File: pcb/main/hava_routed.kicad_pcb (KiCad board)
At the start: 2 copper layers, 32 x 41 mm, 24 parts, among them J1 USB_C_Receptacle_USB2.0_16P, J2 Conn_01x04, SW1 SW_Push, SW2 SW_Push, U1 ESP32-C3-WROOM-02, U2 AP2112K-3.3, U4 USBLC6-2SC6

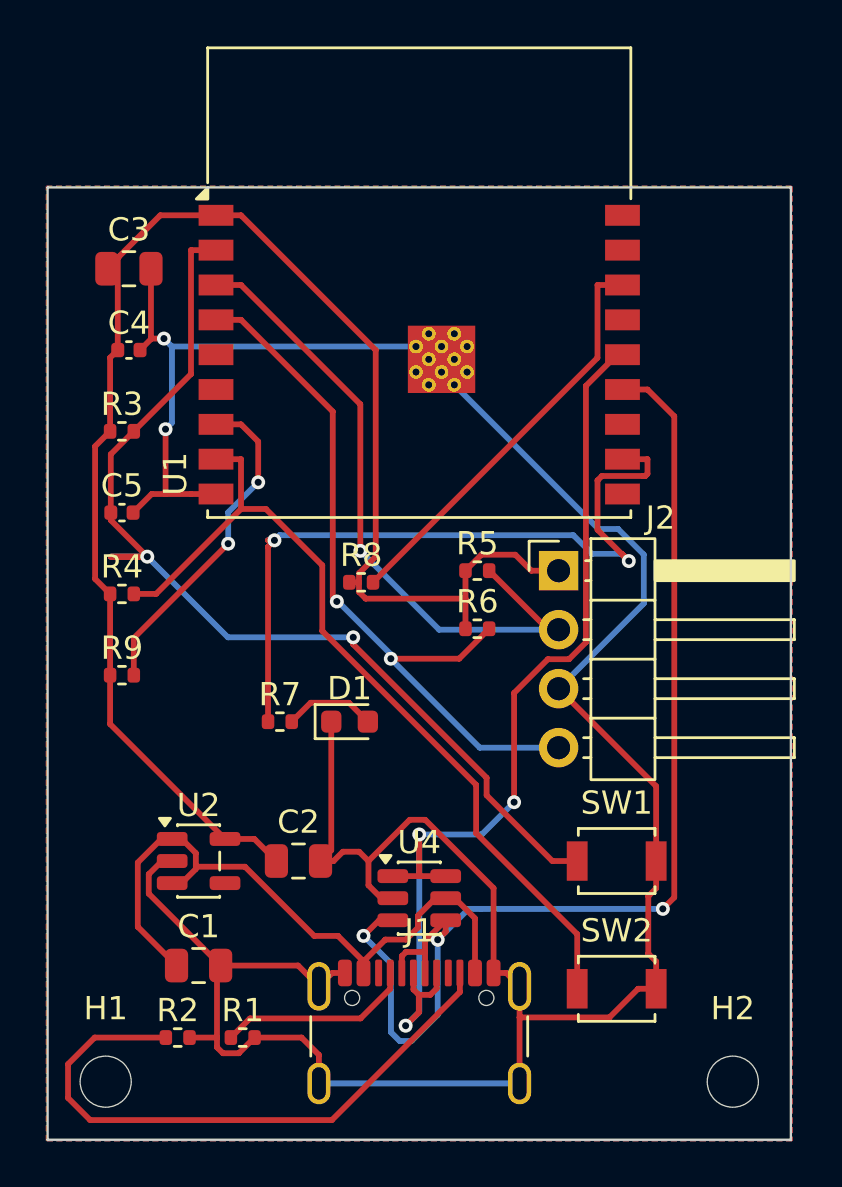
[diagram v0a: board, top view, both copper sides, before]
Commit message: Şematik akışı: kartlar KiCad şematiğinden kuruluyor
Önceden SKiDL netlistinden doğrudan PCB üretiliyordu, arada şematik yoktu.
Artık akış: SKiDL devre tanımı -> KiCad şematiği (hava.kicad_sch) -> ERC ->
şematikten netlist -> PCB yerleşimi -> yol çizimi -> DRC (şematik paritesiyle).

- pcb/tools/sch_gen.py: netlistten KiCad şematiği üretir (İngilizce blok başlıkları)
- pcb/tools/check.sh: şematik üretimi, ERC, netlist karşılaştırması, PDF çıktısı
- pcb/tools/relink_board.py: yolları bozmadan footprint'leri şematiğe yeniden bağlar
- İsimsiz netlere ad verildi: USB_CC1/2, IO2_PU, IO8_PU, LED_A
- Sonuç: ERC 0 hata, DRC 0 ihlal, 0 bağlanmamış pad, şematik-PCB paritesi temiz
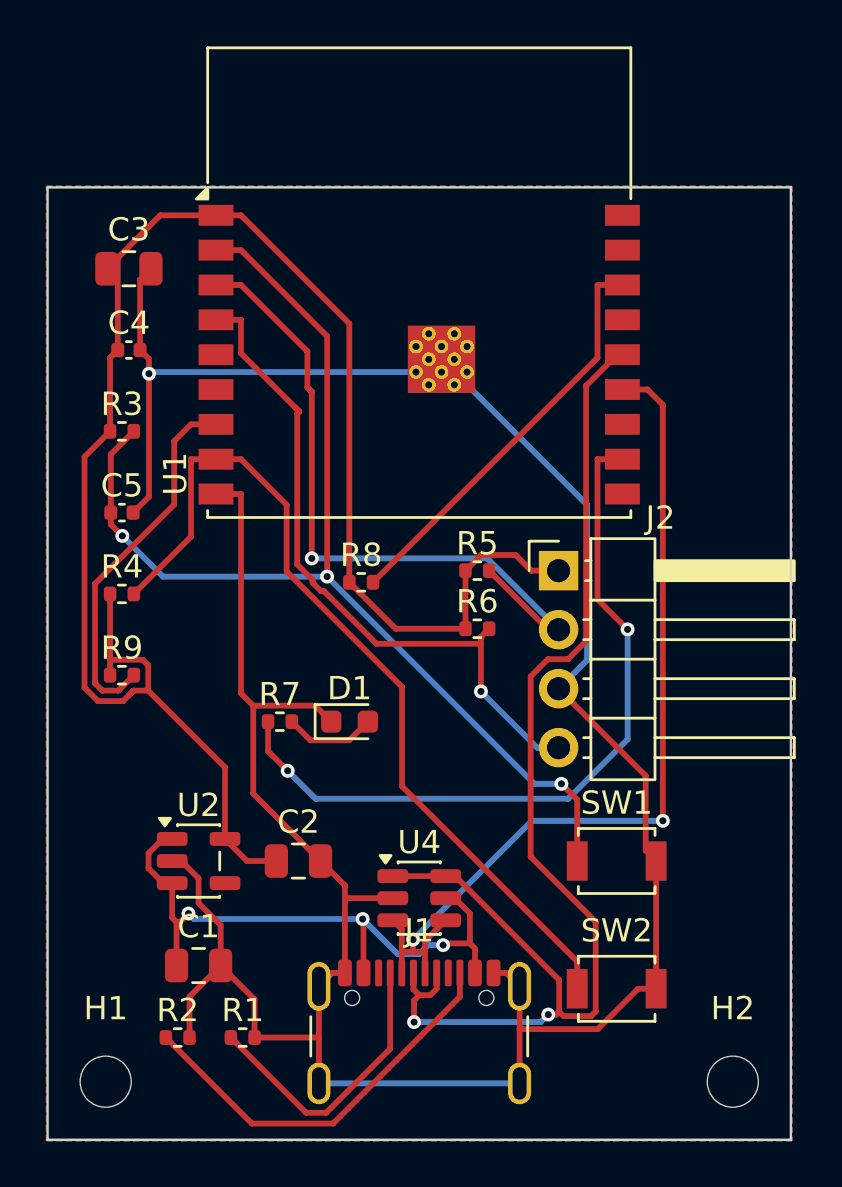
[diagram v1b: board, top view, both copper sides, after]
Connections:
- net BOOT renamed /BOOT
- net EN renamed /EN
- net I2C_SCL renamed /I2C_SCL
- net I2C_SDA renamed /I2C_SDA
- net LED_IO renamed /LED_IO
- net N$1 renamed /USB_CC1
- net N$2 renamed /USB_CC2
- net N$3 renamed /IO2_PU
- net N$4 renamed /IO8_PU
- net N$5 renamed /LED_A
- net USB_DM renamed /USB_DM
- net USB_DP renamed /USB_DP
- J1 pad A8: (no net) -> unconnected-(J1-SBU1-PadA8)
- J1 pad B8: (no net) -> unconnected-(J1-SBU2-PadB8)
- U1 pad 10: (no net) -> unconnected-(U1-IO10-Pad10)
- U1 pad 12: (no net) -> unconnected-(U1-IO21/TXD-Pad12)
- U1 pad 15: (no net) -> unconnected-(U1-IO3-Pad15)
- U1 pad 17: (no net) -> unconnected-(U1-IO1-Pad17)
- U1 pad 18: (no net) -> unconnected-(U1-IO0-Pad18)
- U1 pad 5: (no net) -> unconnected-(U1-IO6-Pad5)
- U1 pad 6: (no net) -> unconnected-(U1-IO7-Pad6)
- U2 pad 4: (no net) -> unconnected-(U2-NC-Pad4)
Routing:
- net /USB_DM: track 51.8 -> 39.4 mm, vias 3 -> 2
- net /USB_DP: track 43.2 -> 54.1 mm, vias 3 -> 2
- net /USB_CC2: track 26.5 -> 17.5 mm
- net +3V3: track 68.3 -> 76.7 mm
- net /USB_CC1: track 8.41 -> 12.6 mm
- net /I2C_SCL: track 31.9 -> 29.5 mm, vias 2 -> 1
- net /LED_IO: track 34.6 -> 32.3 mm
- net +5V: track 28.6 -> 26.8 mm, vias 0 -> 3
- net /I2C_SDA: track 28.6 -> 30.3 mm
- net /IO8_PU: track 14.4 -> 16.0 mm, vias 2 -> 0
- net /EN: track 47.2 -> 48.7 mm, vias 2 -> 3
- net /BOOT: track 36.6 -> 37.8 mm
- net GND: track 136.5 -> 136.4 mm, vias 2 -> 1
